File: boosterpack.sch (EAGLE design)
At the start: 17 parts

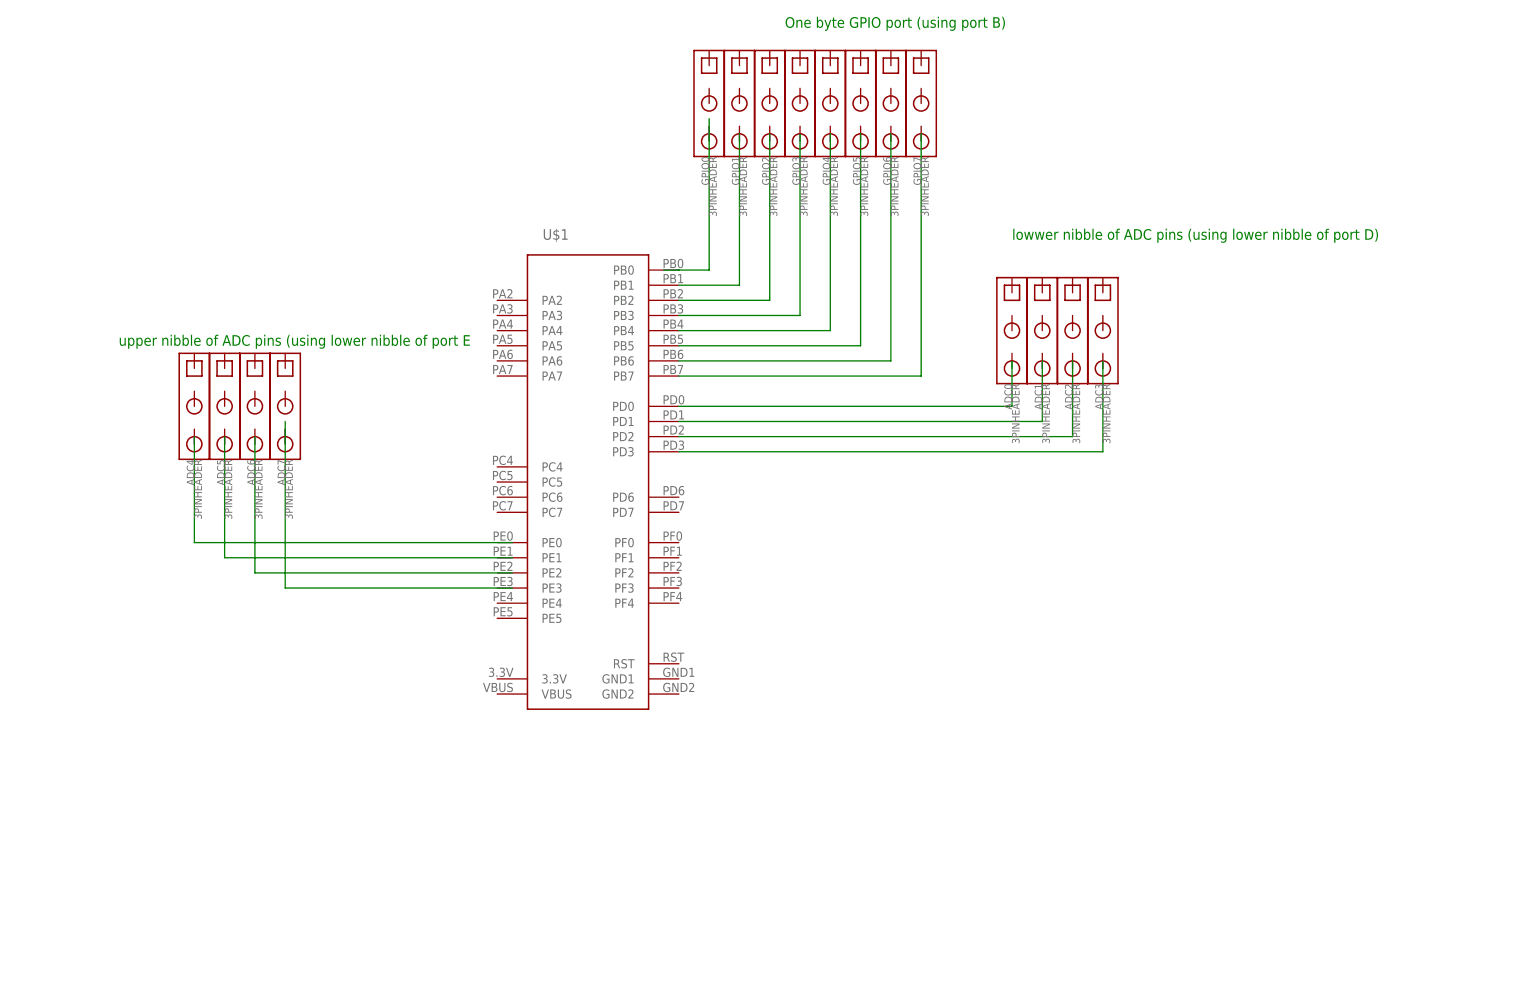
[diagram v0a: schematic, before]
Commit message: added power regulating circiut
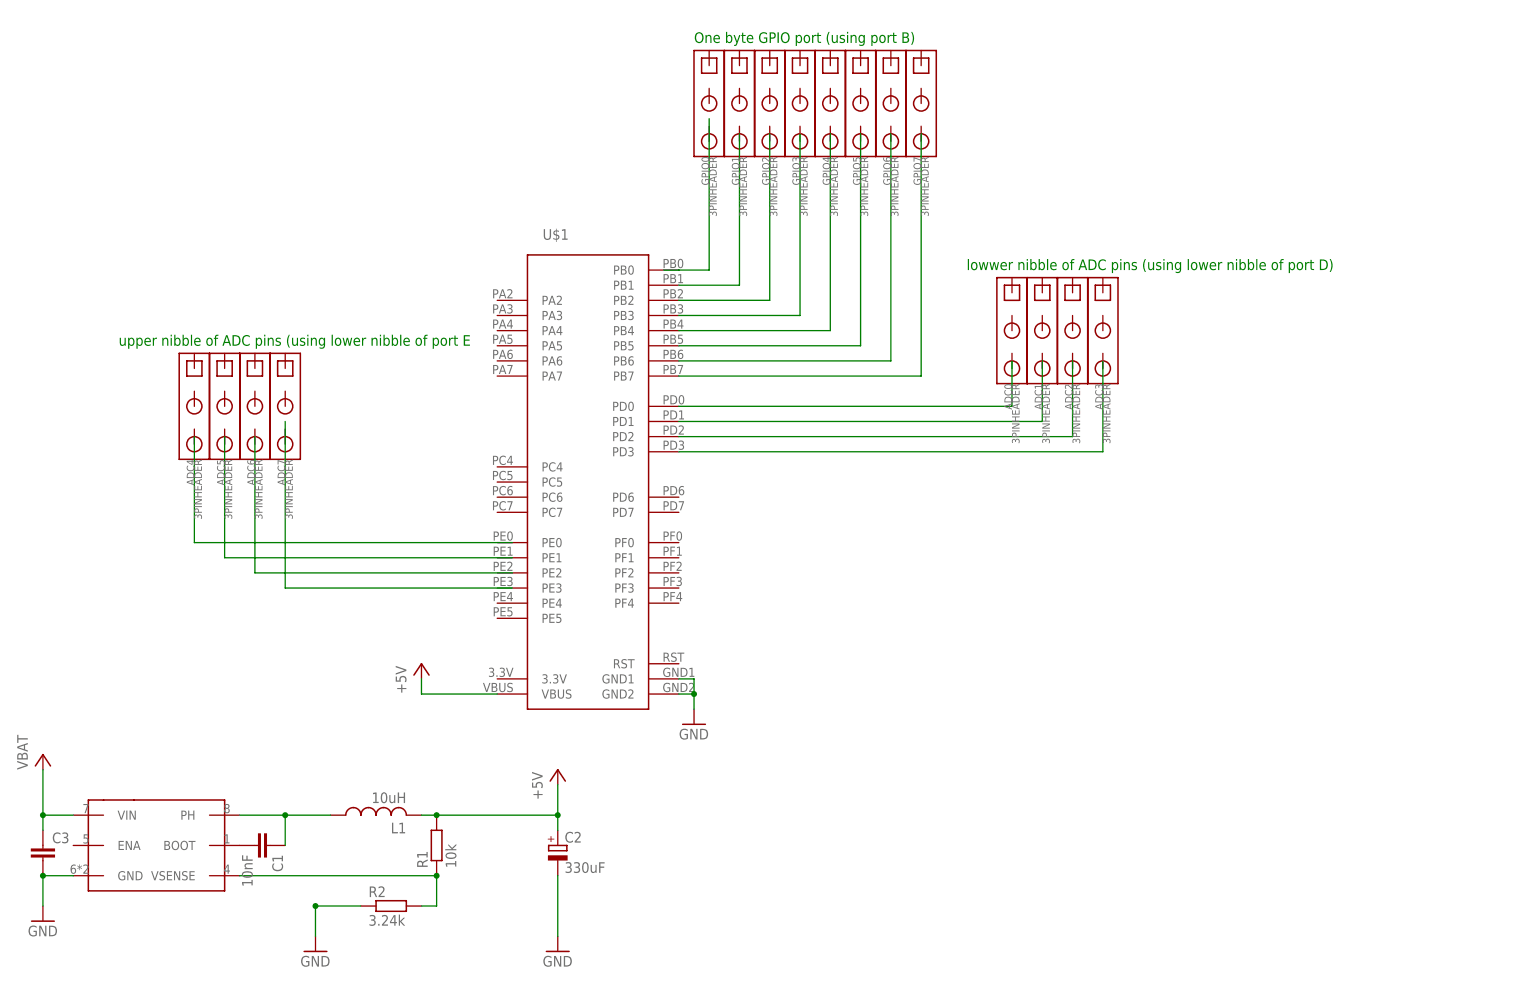
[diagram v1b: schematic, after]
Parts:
- added C1: 10nF, resistor:C-EU025-024X044
- added C2: 330uF, resistor:CPOL-EUB45181A
- added C3: (no value), resistor:C-EU025-024X044
- added L1: 10uH, resistor:L-US0204/5
- added R1: 10k, resistor:R-EU_0204/5
- added R2: 3.24k, resistor:R-EU_0204/5
- added U$2: TPS5450, packages(ti):TPS5450
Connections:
- new net +5V: C2.+, L1.2, R1.2, U$1.VBUS
- new net GND: C2.-, C3.2, R2.1, U$1.GND1, U$1.GND2, U$2.GND
- new net N$10: R1.1, R2.2, U$2.VSENSE
- new net N$11: C1.1, L1.1, U$2.PH
- new net N$9: C1.2, U$2.BOOT
- new net VCC: C3.1, U$2.VIN
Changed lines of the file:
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@@
 <part name="ADC5" library="RASEagleLib" deviceset="3PINHEADER" device=""/>
 <part name="ADC4" library="RASEagleLib" deviceset="3PINHEADER" device=""/>
+<part name="U$2" library="packages(ti)" deviceset="TPS5450" device=""/>
+<part name="P+1" library="supply1" deviceset="+5V" device=""/>
+<part name="P+2" library="supply1" deviceset="VCC" device="" value="VBAT"/>
+<part name="C1" library="resistor" deviceset="C-EU" device="025-024X044" value="10nF"/>
+<part name="L1" library="resistor" deviceset="L-US" device="0204/5" value="10uH"/>
+<part name="R1" library="resistor" deviceset="R-EU_" device="0204/5" value="10k"/>
+<part name="R2" library="resistor" deviceset="R-EU_" device="0204/5" value="3.24k"/>
+<part name="C2" library="resistor" deviceset="CPOL-EU" device="B45181A" value="330uF"/>
+<part name="GND1" library="supply1" deviceset="GND" device=""/>
+<part name="GND2" library="supply1" deviceset="GND" device=""/>
+<part name="GND3" library="supply1" deviceset="GND" device=""/>
+<part name="C3" library="resistor" deviceset="C-EU" device="025-024X044"/>
+<part name="P+3" library="supply1" deviceset="+5V" device=""/>
+<part name="GND4" library="supply1" deviceset="GND" device=""/>
 </parts>
 <sheets>
 <sheet>
 <plain>
-<text x="104.14" y="134.62" size="1.778" layer="91">One byte GPIO port (using port B)</text>
-<text x="142.24" y="99.06" size="1.778" layer="91">lowwer nibble of ADC pins (using lower nibble of port D)</text>
+<text x="88.9" y="132.08" size="1.778" layer="91">One byte GPIO port (using port B)</text>
+<text x="134.62" y="93.98" size="1.778" layer="91">lowwer nibble of ADC pins (using lower nibble of port D)</text>
 <text x="-7.62" y="81.28" size="1.778" layer="91">upper nibble of ADC pins (using lower nibble of port E</text>
 </plain>
@@
 <instance part="ADC5" gate="G$1" x="10.16" y="71.12" rot="R270"/>
 <instance part="ADC4" gate="G$1" x="5.08" y="71.12" rot="R270"/>
+<instance part="U$2" gate="G$1" x="0" y="0"/>
+<instance part="P+1" gate="1" x="66.04" y="10.16"/>
+<instance part="P+2" gate="VCC" x="-20.32" y="12.7"/>
+<instance part="C1" gate="G$1" x="17.78" y="-2.54" rot="R270"/>
+<instance part="L1" gate="G$1" x="35.56" y="2.54" rot="R90"/>
+<instance part="R1" gate="G$1" x="45.72" y="-2.54" rot="R90"/>
+<instance part="R2" gate="G$1" x="38.1" y="-12.7"/>
+<instance part="C2" gate="G$1" x="66.04" y="-2.54"/>
+<instance part="GND1" gate="1" x="66.04" y="-20.32"/>
+<instance part="GND2" gate="1" x="-20.32" y="-15.24"/>
+<instance part="GND3" gate="1" x="25.4" y="-20.32"/>
+<instance part="C3" gate="G$1" x="-20.32" y="-2.54"/>
+<instance part="P+3" gate="1" x="43.18" y="27.94"/>
+<instance part="GND4" gate="1" x="88.9" y="17.78"/>
 </instances>
 <busses>
@@
 </segment>
 </net>
+<net name="N$9" class="0">
+<segment>
+<pinref part="U$2" gate="G$1" pin="BOOT"/>
+<pinref part="C1" gate="G$1" pin="2"/>
+</segment>
+</net>
+<net name="+5V" class="0">
+<segment>
+<pinref part="P+1" gate="1" pin="+5V"/>
+<pinref part="C2" gate="G$1" pin="+"/>
+<wire x1="66.04" y1="7.62" x2="66.04" y2="2.54" width="0.1524" layer="91"/>
+<pinref part="L1" gate="G$1" pin="2"/>
+<wire x1="66.04" y1="2.54" x2="66.04" y2="0" width="0.1524" layer="91"/>
+<wire x1="43.18" y1="2.54" x2="45.72" y2="2.54" width="0.1524" layer="91"/>
+<junction x="66.04" y="2.54"/>
+<junction x="45.72" y="2.54"/>
+<wire x1="45.72" y1="2.54" x2="66.04" y2="2.54" width="0.1524" layer="91"/>
+<pinref part="R1" gate="G$1" pin="2"/>
+</segment>
+<segment>
+<pinref part="U$1" gate="G$1" pin="VBUS"/>
+<pinref part="P+3" gate="1" pin="+5V"/>
+<wire x1="55.88" y1="22.86" x2="43.18" y2="22.86" width="0.1524" layer="91"/>
+<wire x1="43.18" y1="22.86" x2="43.18" y2="25.4" width="0.1524" layer="91"/>
+</segment>
+</net>
+<net name="GND" class="0">
+<segment>
+<pinref part="C2" gate="G$1" pin="-"/>
+<pinref part="GND1" gate="1" pin="GND"/>
+<wire x1="66.04" y1="-7.62" x2="66.04" y2="-17.78" width="0.1524" layer="91"/>
+</segment>
+<segment>
+<pinref part="R2" gate="G$1" pin="1"/>
+<pinref part="GND3" gate="1" pin="GND"/>
+<wire x1="33.02" y1="-12.7" x2="25.4" y2="-12.7" width="0.1524" layer="91"/>
+<wire x1="25.4" y1="-12.7" x2="25.4" y2="-17.78" width="0.1524" layer="91"/>
+<junction x="25.4" y="-12.7"/>
+</segment>
+<segment>
+<pinref part="GND2" gate="1" pin="GND"/>
+<pinref part="C3" gate="G$1" pin="2"/>
+<wire x1="-20.32" y1="-12.7" x2="-20.32" y2="-7.62" width="0.1524" layer="91"/>
+<pinref part="U$2" gate="G$1" pin="GND"/>
+<wire x1="-20.32" y1="-7.62" x2="-15.24" y2="-7.62" width="0.1524" layer="91"/>
+<junction x="-20.32" y="-7.62"/>
+</segment>
+<segment>
+<pinref part="U$1" gate="G$1" pin="GND1"/>
+<pinref part="GND4" gate="1" pin="GND"/>
+<wire x1="86.36" y1="25.4" x2="88.9" y2="25.4" width="0.1524" layer="91"/>
+<wire x1="88.9" y1="25.4" x2="88.9" y2="22.86" width="0.1524" layer="91"/>
+<pinref part="U$1" gate="G$1" pin="GND2"/>
+<wire x1="88.9" y1="22.86" x2="88.9" y2="20.32" width="0.1524" layer="91"/>
+<wire x1="86.36" y1="22.86" x2="88.9" y2="22.86" width="0.1524" layer="91"/>
+<junction x="88.9" y="22.86"/>
+</segment>
+</net>
+<net name="N$10" class="0">
+<segment>
+<pinref part="U$2" gate="G$1" pin="VSENSE"/>
+<pinref part="R1" gate="G$1" pin="1"/>
+<wire x1="12.7" y1="-7.62" x2="45.72" y2="-7.62" width="0.1524" layer="91"/>
+<pinref part="R2" gate="G$1" pin="2"/>
+<wire x1="43.18" y1="-12.7" x2="45.72" y2="-12.7" width="0.1524" layer="91"/>
+<wire x1="45.72" y1="-12.7" x2="45.72" y2="-7.62" width="0.1524" layer="91"/>
+<junction x="45.72" y="-7.62"/>
+</segment>
+</net>
+<net name="N$11" class="0">
+<segment>
+<pinref part="U$2" gate="G$1" pin="PH"/>
+<pinref part="L1" gate="G$1" pin="1"/>
+<wire x1="12.7" y1="2.54" x2="20.32" y2="2.54" width="0.1524" layer="91"/>
+<pinref part="C1" gate="G$1" pin="1"/>
+<wire x1="20.32" y1="2.54" x2="27.94" y2="2.54" width="0.1524" layer="91"/>
+<wire x1="20.32" y1="-2.54" x2="20.32" y2="2.54" width="0.1524" layer="91"/>
+<junction x="20.32" y="2.54"/>
+</segment>
+</net>
+<net name="VCC" class="0">
+<segment>
+<pinref part="U$2" gate="G$1" pin="VIN"/>
+<pinref part="C3" gate="G$1" pin="1"/>
+<wire x1="-15.24" y1="2.54" x2="-20.32" y2="2.54" width="0.1524" layer="91"/>
+<wire x1="-20.32" y1="2.54" x2="-20.32" y2="0" width="0.1524" layer="91"/>
+<pinref part="P+2" gate="VCC" pin="VCC"/>
+<wire x1="-20.32" y1="10.16" x2="-20.32" y2="2.54" width="0.1524" layer="91"/>
+<junction x="-20.32" y="2.54"/>
+</segment>
+</net>

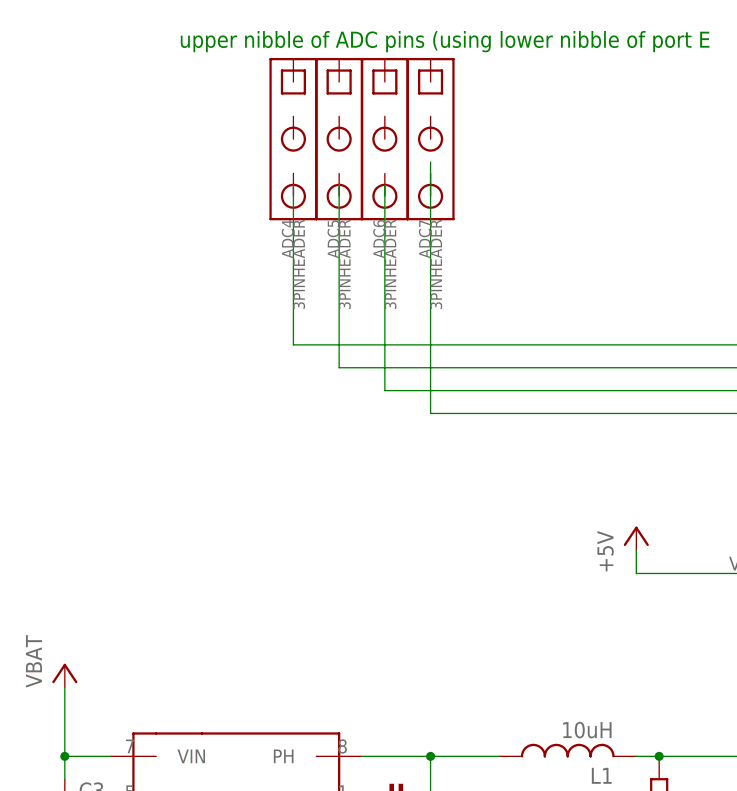
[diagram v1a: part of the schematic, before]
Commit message: new layout for the reg circuit
I feel like explaining my use of the smd inductor
 * it's small ~10mm wide by ~6mm tall
 * it's easy to solder (it's a huge smd part afterall)
 * it's cheip $0.60
 * it makes putting the regulator under the launchpad possible
 * it brings down the surface area by about half compared to other parts
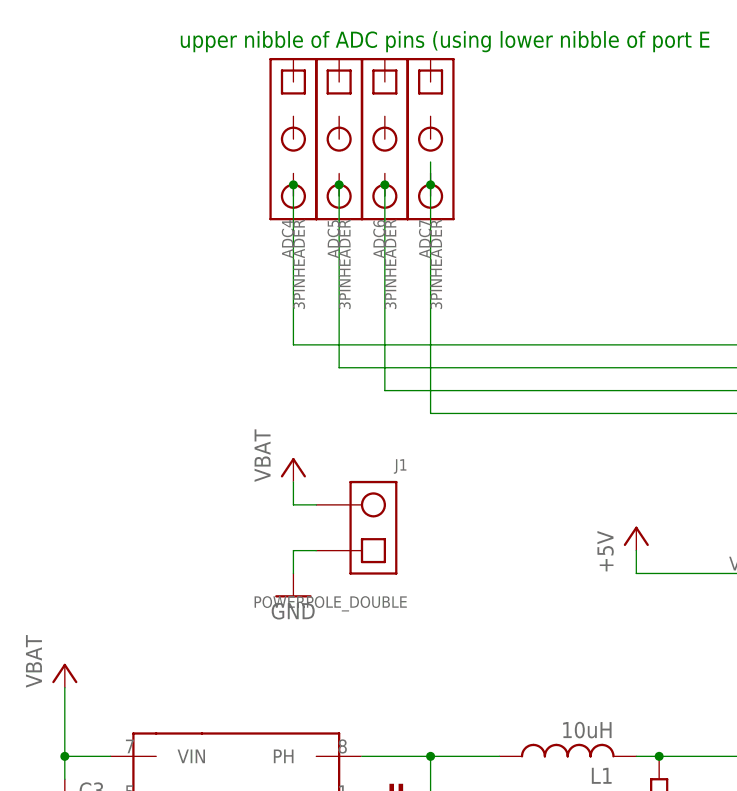
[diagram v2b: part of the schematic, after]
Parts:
- added J1: POWERPOLE_DOUBLE, RASEagleLib:POWERPOLE_DOUBLE
- L1: device resistor:L-US0204/5 -> RASEagleLib:SDR1006
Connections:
- net GND: now also J1.1
- net VCC: now also J1.2
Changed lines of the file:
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@@
 <part name="P+2" library="supply1" deviceset="VCC" device="" value="VBAT"/>
 <part name="C1" library="resistor" deviceset="C-EU" device="025-024X044" value="10nF"/>
-<part name="L1" library="resistor" deviceset="L-US" device="0204/5" value="10uH"/>
+<part name="L1" library="RASEagleLib" deviceset="SDR1006" device="" value="10uH"/>
 <part name="R1" library="resistor" deviceset="R-EU_" device="0204/5" value="10k"/>
 <part name="R2" library="resistor" deviceset="R-EU_" device="0204/5" value="3.24k"/>
@@
 <part name="P+3" library="supply1" deviceset="+5V" device=""/>
 <part name="GND4" library="supply1" deviceset="GND" device=""/>
+<part name="J1" library="RASEagleLib" deviceset="POWERPOLE_DOUBLE" device=""/>
+<part name="GND5" library="supply1" deviceset="GND" device=""/>
+<part name="P+4" library="supply1" deviceset="VCC" device="" value="VBAT"/>
 </parts>
 <sheets>
@@
 <instance part="P+3" gate="1" x="43.18" y="27.94"/>
 <instance part="GND4" gate="1" x="88.9" y="17.78"/>
+<instance part="J1" gate="G$1" x="12.7" y="25.4" rot="R180"/>
+<instance part="GND5" gate="1" x="5.08" y="20.32"/>
+<instance part="P+4" gate="VCC" x="5.08" y="35.56"/>
 </instances>
 <busses>
@@
 <wire x1="58.42" y1="48.26" x2="5.08" y2="48.26" width="0.1524" layer="91"/>
 <wire x1="5.08" y1="48.26" x2="5.08" y2="66.04" width="0.1524" layer="91"/>
+<junction x="5.08" y="66.04"/>
 </segment>
 </net>
@@
 <wire x1="58.42" y1="45.72" x2="10.16" y2="45.72" width="0.1524" layer="91"/>
 <wire x1="10.16" y1="45.72" x2="10.16" y2="66.04" width="0.1524" layer="91"/>
+<junction x="10.16" y="66.04"/>
 </segment>
 </net>
@@
 <wire x1="58.42" y1="43.18" x2="15.24" y2="43.18" width="0.1524" layer="91"/>
 <wire x1="15.24" y1="43.18" x2="15.24" y2="66.04" width="0.1524" layer="91"/>
+<junction x="15.24" y="66.04"/>
 </segment>
 </net>
@@
 <segment>
 <wire x1="58.42" y1="40.64" x2="20.32" y2="40.64" width="0.1524" layer="91"/>
-<wire x1="20.32" y1="40.64" x2="20.32" y2="68.58" width="0.1524" layer="91"/>
+<wire x1="20.32" y1="40.64" x2="20.32" y2="66.04" width="0.1524" layer="91"/>
+<junction x="20.32" y="66.04"/>
+<wire x1="20.32" y1="66.04" x2="20.32" y2="68.58" width="0.1524" layer="91"/>
 </segment>
 </net>
@@
 <junction x="88.9" y="22.86"/>
 </segment>
+<segment>
+<pinref part="J1" gate="G$1" pin="1"/>
+<pinref part="GND5" gate="1" pin="GND"/>
+<wire x1="7.62" y1="25.4" x2="5.08" y2="25.4" width="0.1524" layer="91"/>
+<wire x1="5.08" y1="25.4" x2="5.08" y2="22.86" width="0.1524" layer="91"/>
+</segment>
 </net>
 <net name="N$10" class="0">
@@
 <junction x="-20.32" y="2.54"/>
 </segment>
-</net>
+<segment>
+<pinref part="J1" gate="G$1" pin="2"/>
+<wire x1="7.62" y1="30.48" x2="5.08" y2="30.48" width="0.1524" layer="91"/>
+<wire x1="5.08" y1="30.48" x2="5.08" y2="33.02" width="0.1524" layer="91"/>
+<pinref part="P+4" gate="VCC" pin="VCC"/>
+</segment>
+</net>

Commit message: lots of routing; moustly just routing
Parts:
- added SJ1, SJ2: (no value), jumper:SJ2W
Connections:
- new net ADC5: ADC5.3, U$1.PE1
- new net N$13: ADC4.3, U$1.PE0
- new net N$16: SJ1.3, SJ2.3, U$1.3.3V
- new net N$4: ADC6.3, U$1.PE2
- new net N$5: ADC7.3, U$1.PE3
- new net RIGHTSIDEPOWER: ADC0.2, ADC1.2, ADC2.2, ADC3.2, ADC4.2, ADC5.2, ADC6.2, ADC7.2, SJ1.2
- net +5V: now also SJ1.1, SJ2.1
- net ADC1: now also ADC1.3
- net ADC2: now also ADC2.3
- net ADC3: now also ADC3.3
- net GND: now also ADC0.1, ADC1.1, ADC2.1, ADC3.1, ADC4.1, ADC5.1, ADC6.1, ADC7.1, GPIO0.1, GPIO1.1, GPIO2.1, GPIO3.1, GPIO4.1, GPIO5.1, GPIO6.1, GPIO7.1
- net GPIO0: now also GPIO0.3
- net GPIO1: now also GPIO1.3
- net GPIO2: now also GPIO2.3
- net GPIO3: now also GPIO3.3
- net N$1: now also ADC0.3
- net N$2: now also GPIO4.3
- net N$3: now also GPIO5.3
- net N$6: now also GPIO6.3
- net N$7: now also GPIO0.2, GPIO1.2, GPIO2.2, GPIO3.2, GPIO4.2, GPIO5.2, GPIO6.2, GPIO7.2, SJ2.2; no longer GPIO0.1
- net N$8: now also GPIO7.3
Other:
- note added: "5V regulator circuit"
- moved on the sheet: ADC0, ADC1, ADC2, ADC3, ADC4, ADC5, ADC6, ADC7, GPIO0, GPIO1, GPIO2, GPIO3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
